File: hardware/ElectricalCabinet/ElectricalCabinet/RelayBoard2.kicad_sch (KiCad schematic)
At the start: 28 parts, among them J4 Screw_Terminal_01x06, J5 Screw_Terminal_01x09, K10 G3MB-202P DC5, K11 G3MB-202P DC5, K12 G3MB-202P DC5, K13 G3MB-202P DC5, K14 G3MB-202P DC5, K15 G3MB-202P DC5, K16 G3MB-202P DC5, K9 G3MB-202P DC5, U3 TPIC6B595N

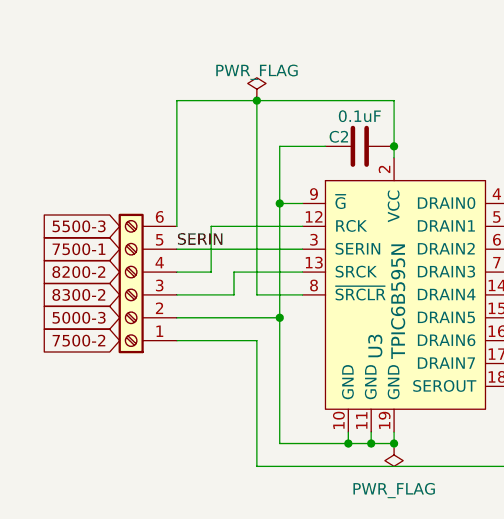
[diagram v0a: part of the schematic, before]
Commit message: Schematic Update
Electrical Cabinet schematic done, this will be the last update unless something else needs to be changed.
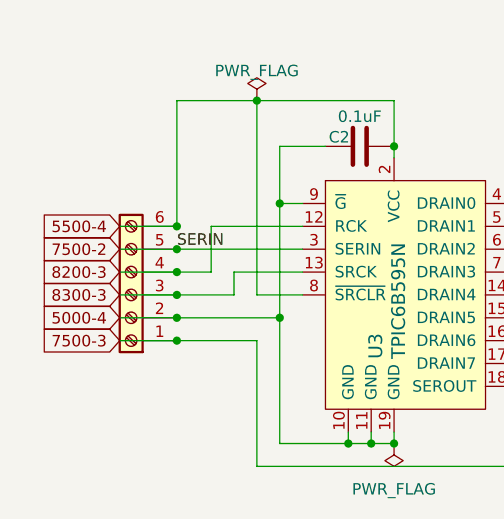
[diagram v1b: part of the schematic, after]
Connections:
- net SERIN is gone; now on net 7500-2: J4.5 (Pin_5), U3.3 (SERIN)
- net 5000-4: now reaches C2.1, J4.2 (Pin_2), U3.10 (GND), U3.11 (GND), U3.19 (GND), U3.9 (~{G})
- net 8200-3: now reaches J4.4 (Pin_4), U3.12 (RCK)
- net 8300-3: now reaches J4.3 (Pin_3), U3.13 (SRCK)
- net 7500-3: now reaches J4.1 (Pin_1), U3.18 (SEROUT)
- net 5500-4: now reaches C2.2, J4.6 (Pin_6), U3.2 (VCC), U3.8 (~{SRCLR})
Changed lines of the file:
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@@
+	)
+	(junction
+		(at 43.18 147.32)
+		(diameter 0)
+		(color 0 0 0 0)
 	)
 	(junction
@@
 	)
 	(junction
+		(at 43.18 142.24)
+		(diameter 0)
+		(color 0 0 0 0)
+	)
+	(junction
+		(at 43.18 144.78)
+		(diameter 0)
+		(color 0 0 0 0)
+	)
+	(junction
 		(at 67.31 158.75)
 		(diameter 0)
@@
 	)
 	(junction
+		(at 43.18 137.16)
+		(diameter 0)
+		(color 0 0 0 0)
+	)
+	(junction
 		(at 101.6 121.92)
 		(diameter 0)
@@
 	)
 	(junction
+		(at 43.18 134.62)
+		(diameter 0)
+		(color 0 0 0 0)
+	)
+	(junction
 		(at 64.77 158.75)
 		(diameter 0)
@@
 	)
 	(junction
+		(at 43.18 139.7)
+		(diameter 0)
+		(color 0 0 0 0)
+	)
+	(junction
 		(at 95.25 124.46)
 		(diameter 0)
@@
 	(wire
 		(pts
+			(xy 36.83 142.24) (xy 43.18 142.24)
+		)
+		(stroke
+			(width 0)
+			(type default)
+		)
+	)
+	(wire
+		(pts
 			(xy 99.06 71.12) (xy 101.6 71.12)
 		)
@@
 	(wire
 		(pts
+			(xy 36.83 137.16) (xy 43.18 137.16)
+		)
+		(stroke
+			(width 0)
+			(type default)
+		)
+	)
+	(wire
+		(pts
 			(xy 80.01 149.86) (xy 95.25 149.86)
 		)
@@
 	(wire
 		(pts
+			(xy 36.83 134.62) (xy 43.18 134.62)
+		)
+		(stroke
+			(width 0)
+			(type default)
+		)
+	)
+	(wire
+		(pts
 			(xy 49.53 139.7) (xy 49.53 142.24)
 		)
@@
 	(wire
 		(pts
+			(xy 36.83 144.78) (xy 43.18 144.78)
+		)
+		(stroke
+			(width 0)
+			(type default)
+		)
+	)
+	(wire
+		(pts
 			(xy 171.45 121.92) (xy 162.56 121.92)
 		)
@@
 	(wire
 		(pts
+			(xy 36.83 139.7) (xy 43.18 139.7)
+		)
+		(stroke
+			(width 0)
+			(type default)
+		)
+	)
+	(wire
+		(pts
 			(xy 86.36 137.16) (xy 80.01 137.16)
+		)
+		(stroke
+			(width 0)
+			(type default)
+		)
+	)
+	(wire
+		(pts
+			(xy 36.83 147.32) (xy 43.18 147.32)
 		)
 		(stroke
@@
 		)
 	)
-	(global_label "5500-3"
+	(global_label "5500-4"
 		(shape input)
 		(at 36.83 134.62 180)
@@
 			)
 		)
-		(property "Ref" "Ref 2102"
+		(property "Ref" "Ref 2103"
 			(at 27.94 134.62 0)
 			(show_name no)
@@
 		)
 	)
-	(global_label "7500-2"
+	(global_label "7500-3"
 		(shape input)
 		(at 36.83 147.32 180)
@@
 			)
 		)
-		(property "Ref" "Ref 334"
+		(property "Ref" "Ref 531"
 			(at 26.67 147.32 0)
 			(show_name no)
@@
 		)
 	)
-	(global_label "8200-2"
+	(global_label "8200-3"
 		(shape input)
 		(at 36.83 139.7 180)
@@
 			)
 		)
-		(property "Ref" "Ref 332"
-			(at 26.67 139.7 0)
+		(property "Ref" "Ref 2502"
+			(at 27.94 139.7 0)
 			(show_name no)
 			(do_not_autoplace no)
@@
 		)
 	)
-	(global_label "7500-1"
+	(global_label "7500-2"
 		(shape input)
 		(at 36.83 137.16 180)
@@
 			)
 		)
-		(property "Ref" "Ref 213"
+		(property "Ref" "Ref 334"
 			(at 26.67 137.16 0)
 			(show_name no)
@@
 		)
 	)
-	(global_label "5000-3"
+	(global_label "5000-4"
 		(shape input)
 		(at 36.83 144.78 180)
@@
 			(justify right)
 		)
-		(property "Intersheetrefs" "333"
+		(property "Intersheetrefs" "5vGND"
 			(at 26.2249 144.78 0)
 			(hide yes)
@@
 			)
 		)
-		(property "Ref" "Ref 333"
+		(property "Ref" "Ref 2003"
 			(at 18.796 144.78 0)
 			(show_name no)
@@
 		)
 	)
-	(global_label "8300-2"
+	(global_label "8300-3"
 		(shape input)
 		(at 36.83 142.24 180)
@@
 			)
 		)
-		(property "Ref" "Ref 2401"
+		(property "Ref" "Ref 2402"
 			(at 27.94 142.24 0)
 			(show_name no)
